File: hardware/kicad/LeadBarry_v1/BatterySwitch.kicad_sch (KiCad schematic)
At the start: 21 parts, among them Q1 SS9014, Q2 BC327, Q3 IRFZ44NSTRLPBF, Q5 IRFZ44NSTRLPBF, Q6 IRFZ44NSTRLPBF

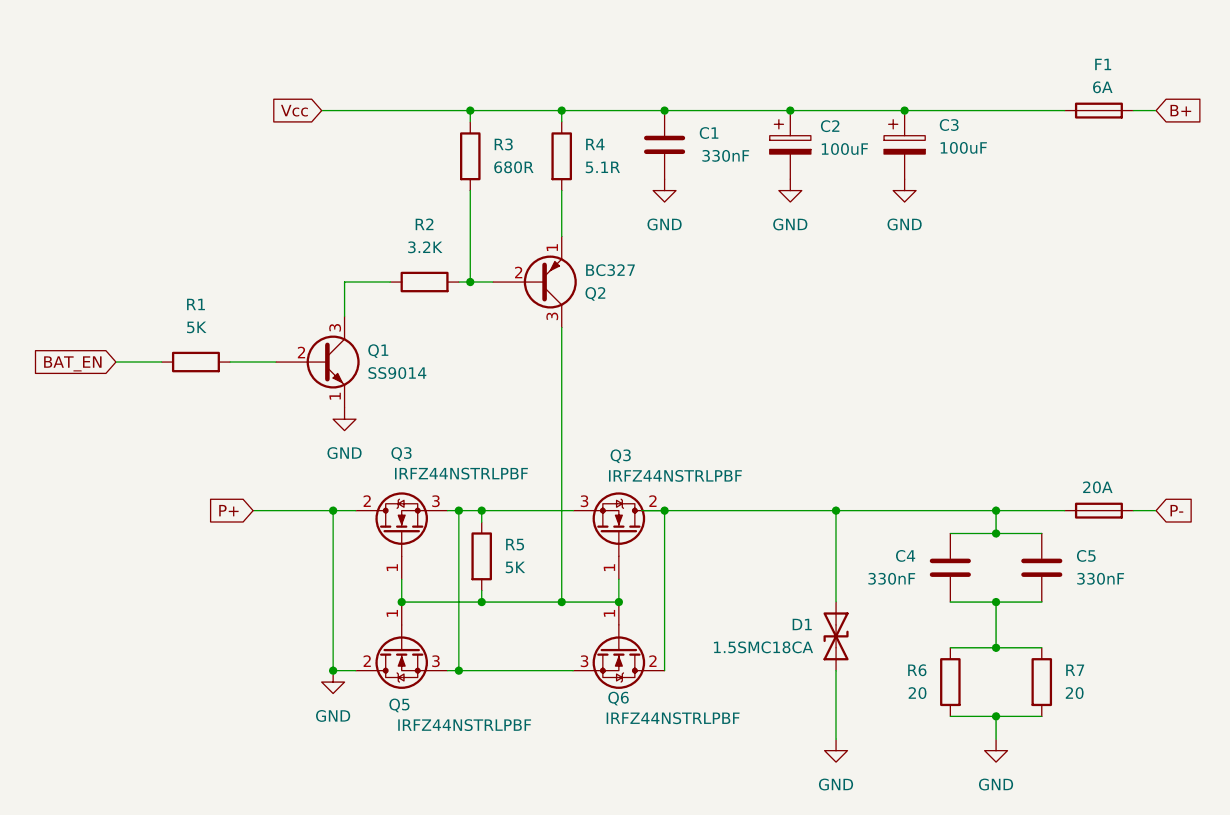
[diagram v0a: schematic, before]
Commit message: fix: P- -> B-, P+ -> P-
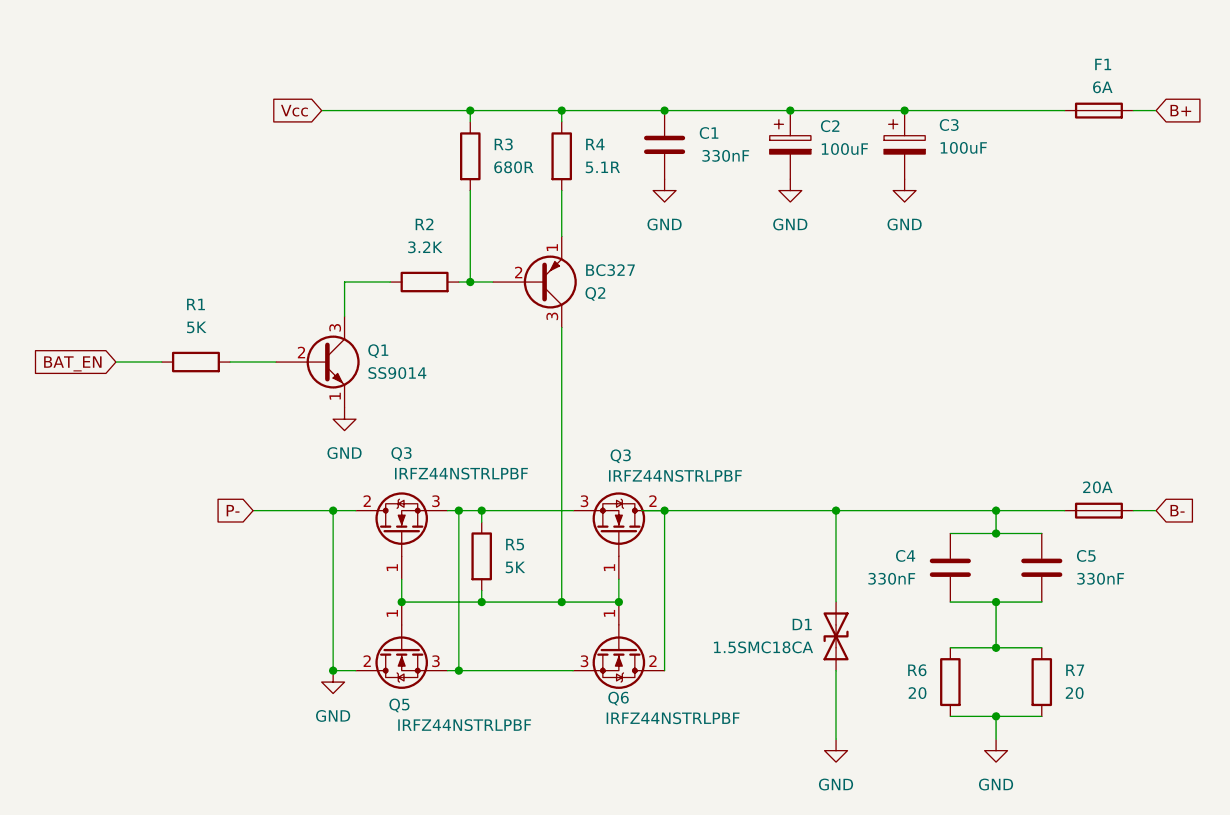
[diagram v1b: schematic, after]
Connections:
- net P- renamed B-
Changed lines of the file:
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@@
 		)
 	)
-	(global_label "P-"
+	(global_label "B-"
 		(shape input)
 		(at 195.58 110.49 0)
@@
 		)
 	)
-	(global_label "P+"
+	(global_label "P-"
 		(shape input)
 		(at 95.25 110.49 180)

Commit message: fix: controlled dc-dc schema
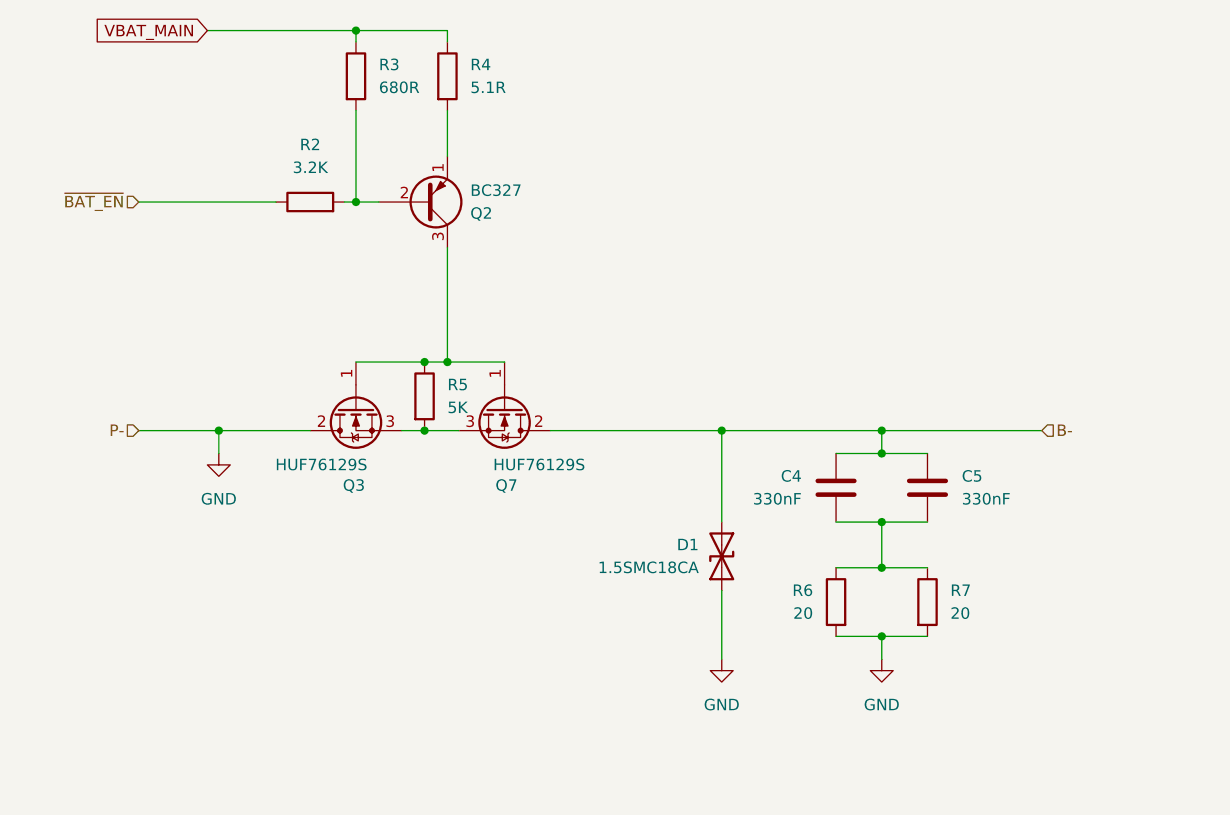
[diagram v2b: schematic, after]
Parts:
- removed C1: 330nF, symbol Device:C
- removed C2, C3: 100uF, symbol Device:C_Polarized
- removed F1: 6A, symbol Device:Fuse
- removed F2: 20A, symbol Device:Fuse
- removed Q1: SS9014, Package_TO_SOT_THT:TO-18-3, symbol Transistor_BJT:ss9014
- removed Q3 (x2), Q5, Q6: IRFZ44NSTRLPBF, Package_TO_SOT_THT:TO-220-3_Vertical, symbol Transistor_FET:IRFZ44NSTRLPBF
- removed R1: 5K, Resistor_THT:R_Axial_DIN0207_L6.3mm_D2.5mm_P10.16mm_Horizontal, symbol Device:R
- added Q3, Q7: HUF76129S, Package_TO_SOT_SMD:TO-263-2, symbol Transistor_FET:IRFZ44NSTRLPBF
- D1: Stock (none) -> https://kosmodrom.ua/zahisniy-diod-supresor/1-5smc18ca-2.ht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
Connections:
- net B-: now also C4.1, C5.1, D1.2 (A2), Q7.2 (D)
- net GND: now also Q3.2 (D)
- net ~{BAT_EN}: now reaches R2.1
- net at Q2.3 (C): now also R5.1, Q3.1 (G), Q7.1 (G); no longer R5.2
- net Vcc renamed VBAT_MAIN
- new net: Q3.3 (S), Q7.3 (S), R5.2
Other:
- moved on the sheet: C4, C5, D1, Q2, R2, R3, R4, R6, R7

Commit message: doc: refactored and enhanced
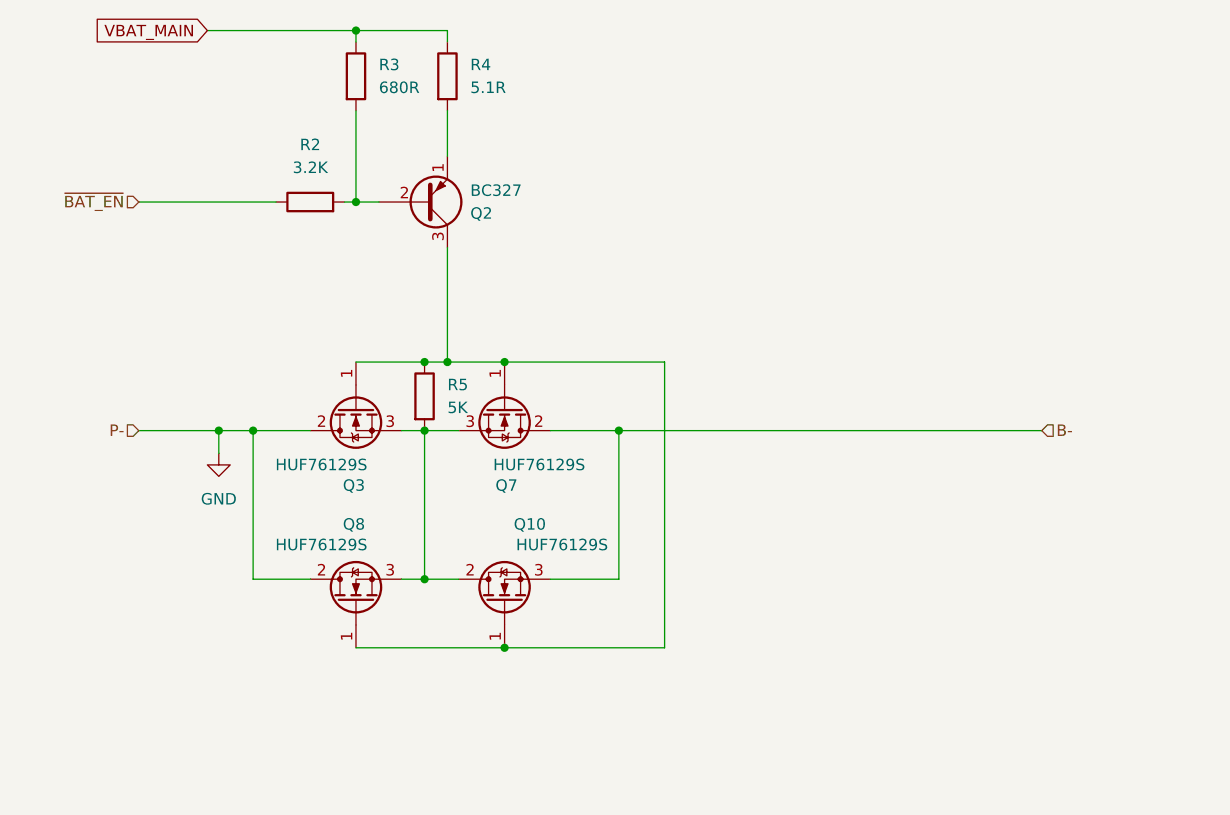
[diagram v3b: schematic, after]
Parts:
- removed C4, C5: 330nF, symbol Device:C
- removed D1: 1.5SMC18CA, Diode_SMD:D_SMC, symbol Diode:1.5SMC18CA
- removed R6, R7: 20, Resistor_THT:R_Axial_DIN0207_L6.3mm_D2.5mm_P10.16mm_Horizontal, symbol Device:R
- added Q10, Q8: HUF76129S, Package_TO_SOT_SMD:TO-263-2, symbol Transistor_FET:IRFZ44NSTRLPBF
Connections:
- net B-: now also Q10.3 (S)
- net GND: now also Q8.2 (D)
- net at Q2.3 (C), Q3.1 (G), Q7.1 (G)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: now also Q10.1 (G), Q8.1 (G)
- net at Q3.3 (S), Q7.3 (S), R5.2: now also Q10.2 (D), Q8.3 (S)

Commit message: fix: PoE sockets and DC output status leds were added
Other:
- title: (none) -> Battery Switch
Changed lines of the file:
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@@
 	(generator_version "8.0")
 	(paper "A4")
+	(title_block
+		(title "Battery Switch")
+		(date "2026-03-21")
+	)
 	(junction
 		(at 114.3 93.98)
